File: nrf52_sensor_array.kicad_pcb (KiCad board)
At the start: 2 copper layers, 48.5 x 21.7 mm, 76 parts, among them IC1 ADS1299, P1 CONN_2, P2 CONN_2, P3 CONN_01X08, U1 TPS2294x, U2 TPS61222, U3 NRF528XX-QFAA, U4 MPU-9250, U5 INA828, U6 INA828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

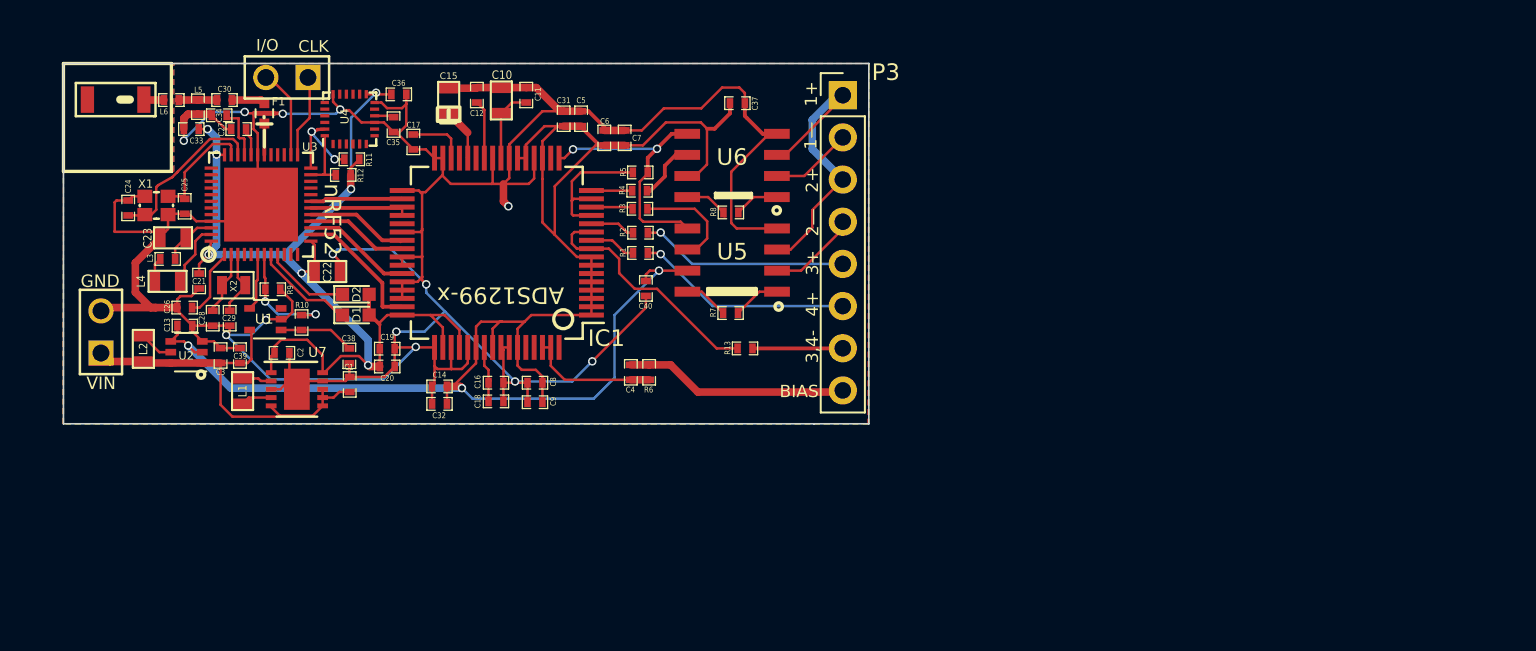
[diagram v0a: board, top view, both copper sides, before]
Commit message: Added battery management (recharging, MCP73831) circuit to device, using 500 mA configuration.
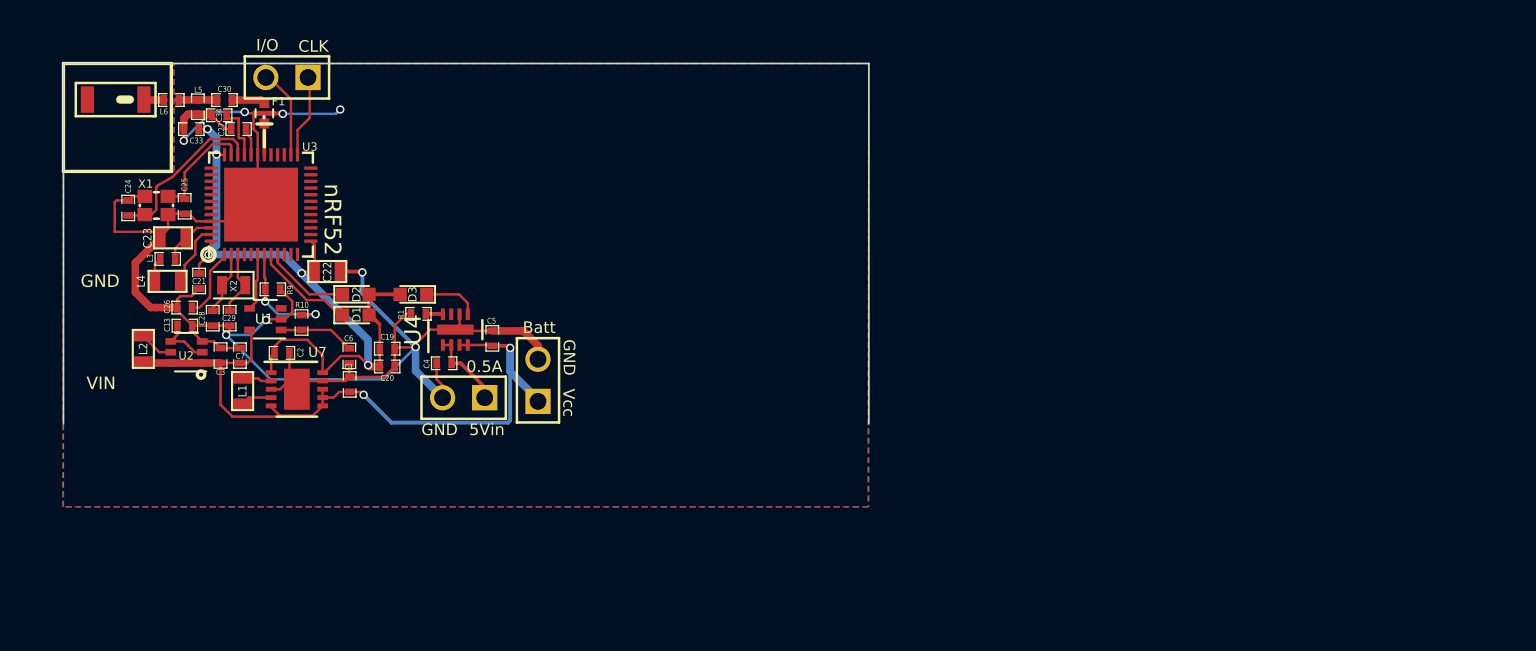
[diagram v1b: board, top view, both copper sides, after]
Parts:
- removed C10: 10uF, SM0603
- removed C11, C18, C31, C32, C9: 0.1uF, SM0402
- removed C12, C14, C16, C17, C37, C40, C8: 1uF, SM0402
- removed C15: 100µF, Power Pads:SM0603_Tant
- removed C35, C36: 100nF, SM0402
- removed the C6 at (298.5, 130.0)
- removed the C7 at (299.7, 130.0)
- removed IC1: ADS1299, Housings_QFP:TQFP-64_10x10mm_Pitch0.5mm
- removed R11, R12, R7, R8: 10k, SM0402
- removed R13, R2, R3, R4, R5: 30k, SM0402
- removed R6: 1MΩ, SM0402
- removed U5, U6: INA828, INA828:SOIC_8_4.9mm_x_3.91
- added D3: LED, LEDs:LED_0603, F.Cu at (287.0, 139.4)
- C4: value 1.0nF -> 4.7uF
- C5: value 1uF -> 4.7uF
- P3: value CONN_01X08 -> CONN_2; footprint Pin_Headers:Pin_Header_Straight_1x08_Pitch2.54mm -> PIN_ARRAY_2X1
- R1: value 30k -> 2k
- U4: value MPU-9250 -> MCP73831; footprint Housings_DFN_QFN:QFN-24_3x3mm_Pitch0.4mm -> Housings_DFN_QFN:DFN-8-1EP_2x3mm_Pitch0.5mm
- moved P3 25.1 mm to (294.5, 144.6), turned to 90 degrees
- moved P1 22.2 mm to (290.0, 145.6), turned to 180 degrees
- moved C5 14.3 mm to (291.7, 142.1)
- moved U4 14.2 mm to (289.5, 141.5)
- moved R1 13.9 mm to (287.3, 140.6)
- moved C4 11.3 mm to (288.8, 143.6), turned to 0 degrees
- renumbered C38 to C6, C39 to C7
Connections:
- C4 pad 1: Net-(C4-Pad1) -> AVSS
- C4 pad 2: /BIASIN -> 5V_in_charge
- C5 pad 2: AVDD -> VCC
- P1 pad 1: VCC -> 5V_in_charge
- P3 pad 1: /REF_ELECTRODE -> VCC
- P3 pad 2: /IN1- -> AVSS
- R1 pad 1: Net-(IC1-Pad10) -> AVSS
- R1 pad 2: /IN4 -> Net-(R1-Pad2)
- U3 pad 23: /SDI -> Net-(U3-Pad23)
- U3 pad 24: /SCL -> Net-(U3-Pad24)
- U4 pad 1: Net-(U4-Pad1) -> 5V_in_charge
- U4 pad 2: Net-(U4-Pad2) -> 5V_in_charge
- U4 pad 3: Net-(U4-Pad3) -> VCC
- U4 pad 4: Net-(U4-Pad4) -> VCC
- U4 pad 6: Net-(U4-Pad6) -> AVSS
- U4 pad 8: Net-(U4-Pad8) -> Net-(R1-Pad2)
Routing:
- net AVSS: track 230.4 -> 125.6 mm, vias 13 -> 8
- net AVDD: track 104.2 -> 3.29 mm, vias 3 -> 0
- net DVDD: track 66.6 -> 44.1 mm, vias 7 -> 5
- net VCC: track 24.8 -> 43.9 mm, vias 0 -> 2
- net /REF_ELECTRODE: track 18.8 -> 0.00 mm
- net /IN12-: track 16.1 -> 0.00 mm, vias 2 -> 0
- net /IN3N: track 15.0 -> 0.00 mm
- net /BIASIN: track 13.5 -> 0.00 mm
- net /IN4: track 13.1 -> 0.00 mm, vias 1 -> 0
- net /IN3: track 12.5 -> 0.00 mm, vias 1 -> 0
- net /IN1N: track 8.31 -> 0.00 mm
- net /~DRDY: track 8.13 -> 0.00 mm
- net Net-(C4-Pad1): track 8.02 -> 0.00 mm
- net /SCL: track 6.80 -> 0.00 mm, vias 2 -> 0
- net /DOUT: track 6.64 -> 0.00 mm
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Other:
- outline, holes or cut-outs redrawn
- board text added: "0.5A"
- board text added: "5Vin"
- board text added: "Batt"
- board text added: "Vcc"
- board text removed: "1+"
- board text removed: "1—"
- board text removed: "2+"
- board text removed: "2—"
- board text removed: "3+"
- board text removed: "3,4-"
- board text removed: "4+"
- board text removed: "ADS1299-x"
- board text removed: "BIAS"
- board text removed: "nRF52-ADS1299-4 with MPU ExG Prototype v3.0 Yeo GaTech BNE Lab"

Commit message: Updated schematic with all components. Plan is to replace multiplexers with ADG1606 (single supply), and get rid of -5V regulator.
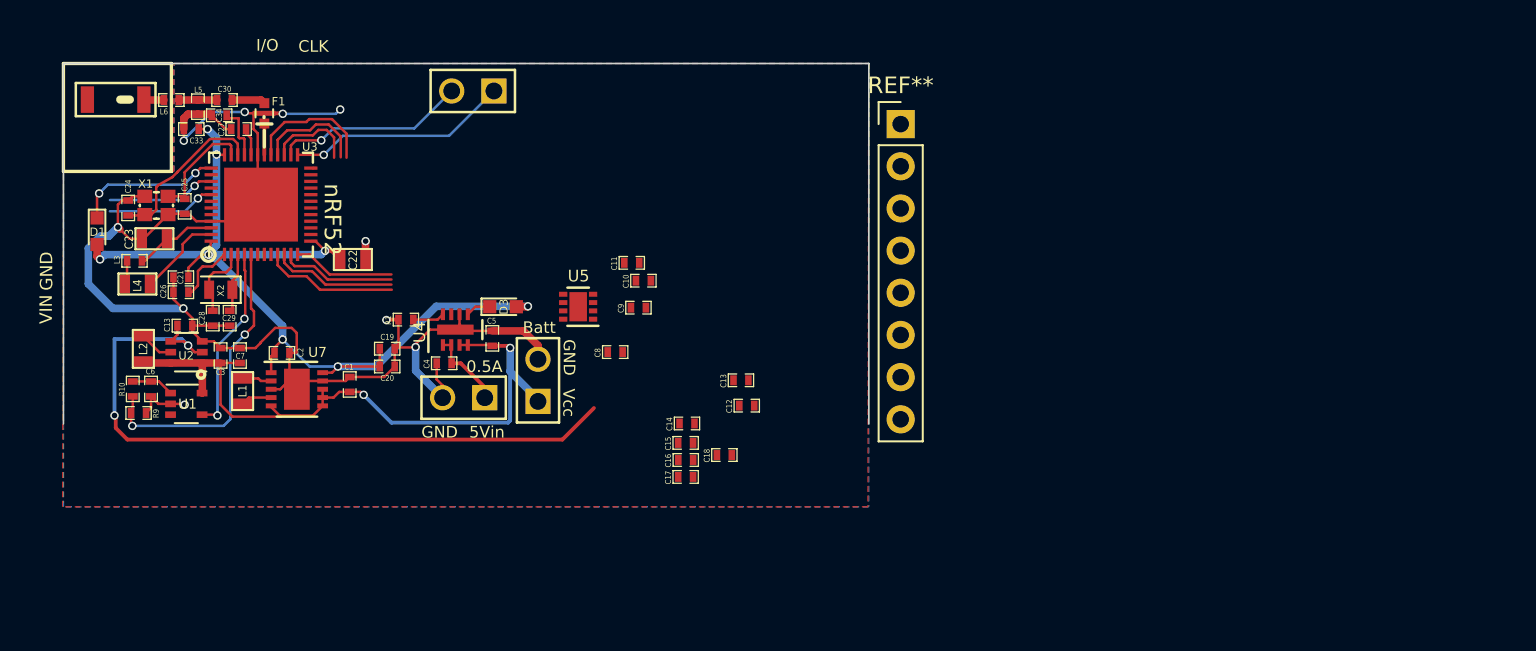
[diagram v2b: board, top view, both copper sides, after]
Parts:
- removed D2: LED, LEDs:LED_0603
- added C10: 4.7uF, SM0402, F.Cu at (300.8, 138.6)
- added C11: 1uF, SM0402, F.Cu at (300.1, 137.5)
- added C12: 4.7uF, SM0402, F.Cu at (307.1, 146.1)
- added C13: 4.7uF, SM0402, F.Cu at (306.7, 144.6)
- added C14: 4.7uF, SM0402, F.Cu at (303.5, 147.2)
- added C15: 4.7uF, SM0402, F.Cu at (303.4, 148.3)
- added C16: 4.7uF, SM0402, F.Cu at (303.4, 149.4)
- added C17: 4.7uF, SM0402, F.Cu at (303.4, 150.4)
- added C18: 4.7uF, SM0402, F.Cu at (305.7, 149.1)
- added C8: 4.7uF, SM0402, F.Cu at (299.1, 142.9)
- added C9: 4.7uF, SM0402, F.Cu at (300.5, 140.2)
- added REF**: Pin_Header_Straight_1x08_Pitch2.54mm, Pin_Headers:Pin_Header_Straight_1x08_Pitch2.54mm, F.Cu at (316.3, 129.2)
- added U5: LM27761, Housings_DFN_QFN:DFN-8-1EP_2x2mm_Pitch0.5mm, F.Cu at (296.9, 140.2)
- moved D1 16.4 mm to (267.9, 135.6), turned to 270 degrees
- moved C6 12.1 mm to (271.2, 145.1)
- moved P2 11.2 mm to (290.6, 127.2)
- moved R9 11.0 mm to (270.4, 146.6)
- moved R10 10.9 mm to (270.1, 145.1), turned to 90 degrees
- moved U1 6.98 mm to (273.3, 146.0), turned to 0 degrees
- moved D3 5.45 mm to (292.4, 140.2), turned to 0 degrees
- moved L3 2.00 mm to (270.2, 137.4)
- moved L4 1.82 mm to (270.4, 138.8)
- moved C22 1.70 mm to (283.3, 137.3)
- moved C23 1.12 mm to (271.4, 136.1)
- moved C21 1.12 mm to (273.0, 138.4), turned to 0 degrees
- moved C26 0.95 mm to (273.0, 139.3)
- moved R1 0.83 mm to (286.5, 140.9)
- moved X2 0.82 mm to (275.4, 139.1)
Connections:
- D1 pad 1: /LED2 -> /LED1
- U3 pad 37: Net-(U3-Pad37) -> /LED1
- U3 pad 4: Net-(U3-Pad4) -> /LOAD_SW_CTRL
- U3 pad 5: Net-(U3-Pad5) -> /AIN_BAT_DIV_VOLTAGE
- U3 pad 6: /LOAD_SW_CTRL -> Net-(U3-Pad6)
- U3 pad 7: /AIN_BAT_DIV_VOLTAGE -> Net-(U3-Pad7)
- U3 pad 8: /LED2 -> Net-(U3-Pad8)
- U3 pad 9: /LED3 -> Net-(U3-Pad9)
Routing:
- net AVDD: track 3.29 -> 43.1 mm, vias 0 -> 2
- net DVDD: track 44.1 -> 60.7 mm, vias 5 -> 8
- net AVSS: track 125.6 -> 110.8 mm, vias 8 -> 10
- net /AIN_BAT_DIV_VOLTAGE: track 7.09 -> 18.5 mm
- net /LED1: track 0.00 -> 8.91 mm, vias 0 -> 2
- net /SWDCLK: track 5.27 -> 13.7 mm, vias 0 -> 1
- net Net-(U3-Pad9): track 0.00 -> 8.14 mm
- net Net-(U3-Pad29): track 0.00 -> 7.93 mm
- net /LOAD_SW_CTRL: track 3.45 -> 11.4 mm, vias 0 -> 2
- net Net-(U3-Pad10): track 0.00 -> 7.50 mm
- net Net-(U3-Pad11): track 0.00 -> 6.96 mm
- net Net-(U3-Pad28): track 0.00 -> 6.63 mm
- net Net-(U3-Pad39): track 0.00 -> 6.57 mm, vias 0 -> 1
- net Net-(U3-Pad41): track 0.00 -> 6.51 mm, vias 0 -> 1
- net /SWDIO: track 5.41 -> 11.6 mm, vias 0 -> 1
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
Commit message: Removed old muxes and -5V reguator. Updated schematic and added ADG1606, and 2 rows of headers.
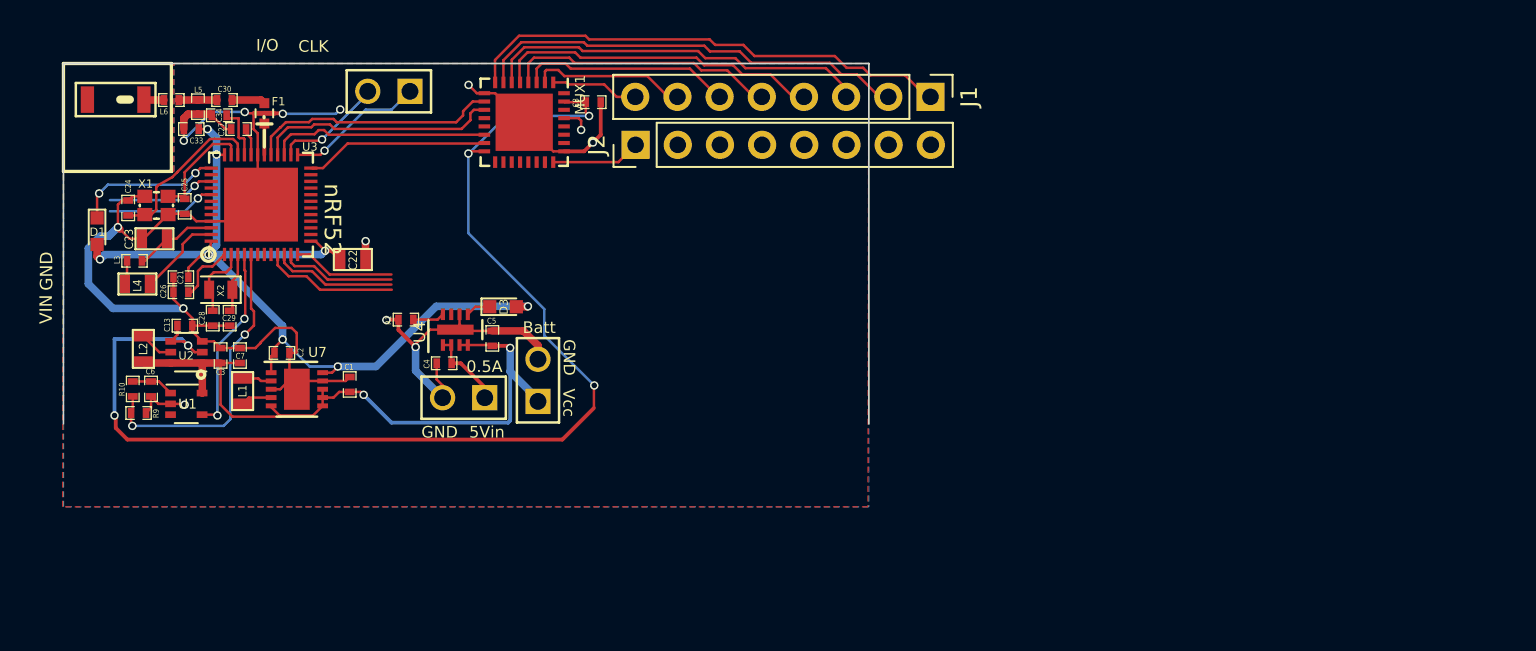
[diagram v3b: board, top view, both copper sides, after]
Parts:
- removed C10, C12, C14, C15, C16, C17, C18, C9: 4.7uF, SM0402
- removed C11, C19: 1uF, SM0402
- removed the C13 at (306.7, 144.6)
- removed C20: 0.1uF, SM0402
- removed REF**: Pin_Header_Straight_1x08_Pitch2.54mm, Pin_Headers:Pin_Header_Straight_1x08_Pitch2.54mm
- removed U5: LM27761, Housings_DFN_QFN:DFN-8-1EP_2x2mm_Pitch0.5mm
- added J1: CONN_01X08, Pin_Headers:Pin_Header_Straight_1x08_Pitch2.54mm, F.Cu at (318.1, 127.5)
- added J2: CONN_01X08, Pin_Headers:Pin_Header_Straight_1x08_Pitch2.54mm, F.Cu at (300.4, 130.4)
- added MUX1: ADG1606, Housings_DFN_QFN:QFN-32-1EP_5x5mm_Pitch0.5mm, F.Cu at (293.6, 129.0)
- moved C8 15.1 mm to (297.8, 127.8)
- moved P2 5.06 mm to (285.5, 127.2)
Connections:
- net /DIN renamed Net-(U3-Pad19)
- net /DOUT renamed Net-(U3-Pad15)
- net /SPI_SCLK renamed Net-(U3-Pad16)
- net /SPI_~CS renamed Net-(U3-Pad17)
- net /~DRDY renamed Net-(U3-Pad14)
- net /~PWDN/RESET renamed Net-(U3-Pad18)
- U3 pad 24: Net-(U3-Pad24) -> /ctr_m1_a0
- U3 pad 27: Net-(U3-Pad27) -> /ctr_m1_a1
- U3 pad 28: Net-(U3-Pad28) -> /ctr_m1_a2
- U3 pad 29: Net-(U3-Pad29) -> /ctr_m1_a3
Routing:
- net AVDD: track 43.1 -> 73.1 mm, vias 2 -> 5
- net Net-(J1-Pad1): track 0.00 -> 29.7 mm
- net Net-(J1-Pad2): track 0.00 -> 26.3 mm
- net Net-(J1-Pad3): track 0.00 -> 23.3 mm
- net Net-(J1-Pad4): track 0.00 -> 19.8 mm
- net Net-(J1-Pad5): track 0.00 -> 16.3 mm
- net /ctr_m1_a3: track 0.00 -> 15.1 mm
- net /ctr_m1_a2: track 0.00 -> 14.6 mm
- net /ctr_m1_a1: track 0.00 -> 13.3 mm
- net Net-(J1-Pad6): track 0.00 -> 12.8 mm
- net /ctr_m1_a0: track 0.00 -> 11.3 mm
- net AVSS: track 110.8 -> 120.4 mm, vias 10 -> 12
- net Net-(J1-Pad7): track 0.00 -> 9.35 mm
- net Net-(U3-Pad29): track 7.93 -> 0.00 mm
- net Net-(U3-Pad28): track 6.63 -> 0.00 mm
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
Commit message: Added ADC: ADS1220, added 2/3 Multiplexers (ADG1606)
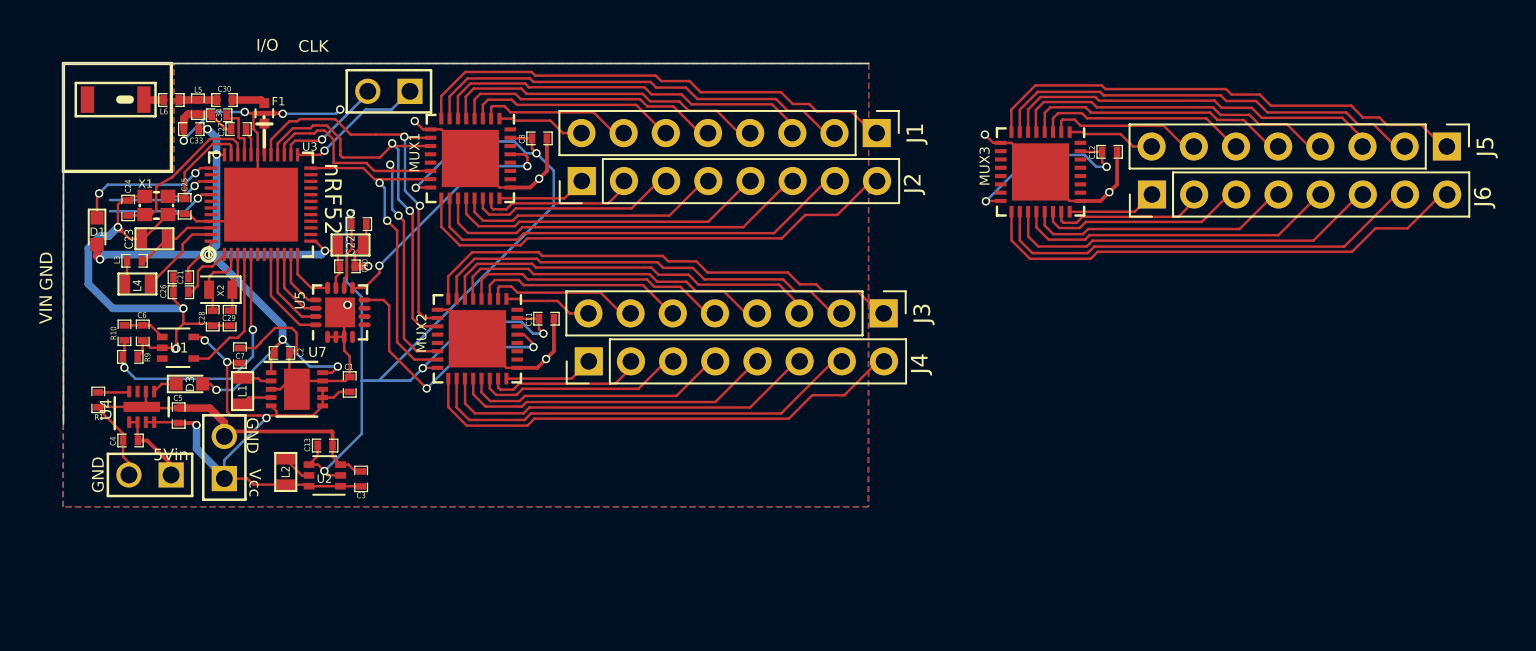
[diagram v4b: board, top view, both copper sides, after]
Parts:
- added C10: 0.1uF, SM0402, F.Cu at (283.0, 137.7)
- added C11: 4.7uF, SM0402, F.Cu at (295.0, 140.9)
- added C12: 4.7uF, SM0402, F.Cu at (328.9, 130.8)
- added C9: 0.1uF, SM0402, F.Cu at (283.7, 135.2)
- added J3: CONN_01X08, Pin_Headers:Pin_Header_Straight_1x08_Pitch2.54mm, F.Cu at (315.3, 140.6)
- added J4: CONN_01X08, Pin_Headers:Pin_Header_Straight_1x08_Pitch2.54mm, F.Cu at (297.5, 143.4)
- added J5: CONN_01X08, Pin_Headers:Pin_Header_Straight_1x08_Pitch2.54mm, F.Cu at (349.2, 130.5)
- added J6: CONN_01X08, Pin_Headers:Pin_Header_Straight_1x08_Pitch2.54mm, F.Cu at (331.5, 133.4)
- added MUX2: ADG1606, Housings_DFN_QFN:QFN-32-1EP_5x5mm_Pitch0.5mm, F.Cu at (290.8, 142.1)
- added MUX3: ADG1606, Housings_DFN_QFN:QFN-32-1EP_5x5mm_Pitch0.5mm, F.Cu at (324.8, 132.0)
- added U5: ADS1220, Housings_DFN_QFN:QFN-16-1EP_3x3mm_Pitch0.5mm, F.Cu at (282.6, 140.5)
- moved C5 19.5 mm to (272.8, 146.7)
- moved P3 19.5 mm to (275.6, 149.2)
- moved C4 19.5 mm to (269.9, 148.2)
- moved D3 19.5 mm to (273.5, 144.8)
- moved P1 19.5 mm to (271.1, 150.3)
- moved U4 19.5 mm to (270.6, 146.2)
- moved R1 19.1 mm to (268.0, 145.8), turned to 90 degrees
- moved L2 11.3 mm to (279.3, 150.1)
- moved C3 11.3 mm to (283.8, 150.5)
- moved U2 11.2 mm to (281.6, 150.3)
- moved C13 11.1 mm to (281.7, 148.5)
- moved J2 3.91 mm to (297.1, 132.6)
- moved C8 3.91 mm to (294.6, 130.0)
- moved J1 3.91 mm to (314.9, 129.7)
- moved MUX1 3.91 mm to (290.4, 131.2)
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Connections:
- U3 pad 10: Net-(U3-Pad10) -> /DIN
- U3 pad 11: Net-(U3-Pad11) -> /DOUT
- U3 pad 12: Net-(U3-Pad12) -> /~DRDY
- U3 pad 8: Net-(U3-Pad8) -> /SPI_~CS
- U3 pad 9: Net-(U3-Pad9) -> /SPI_SCLK
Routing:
- net AVSS: track 120.4 -> 162.7 mm, vias 12 -> 14
- net Net-(J4-Pad8): track 0.00 -> 30.0 mm
- net Net-(J6-Pad8): track 0.00 -> 30.0 mm
- net Net-(J2-Pad8): track 0.00 -> 30.0 mm
- net Net-(J3-Pad1): track 0.00 -> 29.7 mm
- net Net-(J5-Pad1): track 0.00 -> 29.7 mm
- net Net-(J4-Pad7): track 0.00 -> 26.7 mm
- net Net-(J2-Pad7): track 0.00 -> 26.7 mm
- net Net-(J6-Pad7): track 0.00 -> 26.7 mm
- net Net-(J5-Pad2): track 0.00 -> 26.3 mm
- net Net-(J3-Pad2): track 0.00 -> 26.3 mm
- net Net-(J3-Pad3): track 0.00 -> 23.3 mm
- net Net-(J5-Pad3): track 0.00 -> 23.3 mm
- net Net-(J6-Pad6): track 0.00 -> 23.2 mm
- net Net-(J4-Pad6): track 0.00 -> 23.2 mm
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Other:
- outline, holes or cut-outs redrawn
- board text removed: "0.5A"
- board text removed: "Batt"

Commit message: Completed PCB.
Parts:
- moved C12 40.1 mm to (294.6, 151.7)
- moved J5 40.1 mm to (314.9, 151.3)
- moved MUX3 40.1 mm to (290.5, 152.9)
- moved J6 40.1 mm to (297.2, 154.2)
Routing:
- net AVSS: track 162.7 -> 217.4 mm, vias 14 -> 16
- net /ctr_m1_a0: track 21.0 -> 42.5 mm, vias 2 -> 3
- net /ctr_m1_a1: track 25.2 -> 46.1 mm, vias 2 -> 3
- net /ctr_m1_a2: track 25.0 -> 44.3 mm, vias 2 -> 3
- net /ctr_m1_a3: track 23.8 -> 42.7 mm, vias 2 -> 3
- net /m3_D_out: track 0.00 -> 17.4 mm, vias 0 -> 2
- net AVDD: track 83.2 -> 96.8 mm
- net /m1_D_out: track 15.5 -> 18.7 mm
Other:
- board size 48.5 x 21.7 mm -> 55.5 x 33.1 mm
